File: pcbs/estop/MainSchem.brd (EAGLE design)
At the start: 94.9 x 61.8 mm, 41 parts, among them Q1 FDBL9401-F085, Q2 FDBL9401-F085, U1 FAN3100T, U2 FAN3100T

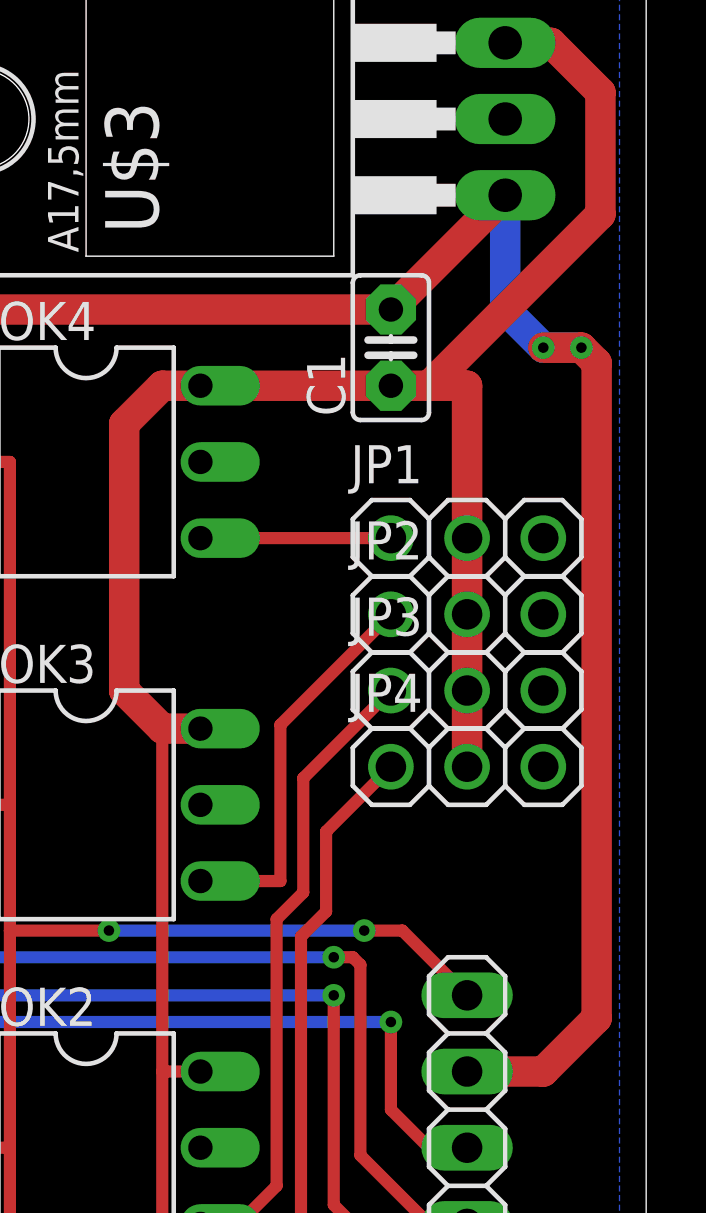
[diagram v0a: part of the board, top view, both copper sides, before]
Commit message: Fixed bugs in e-stop board for if I re-order them eventually.
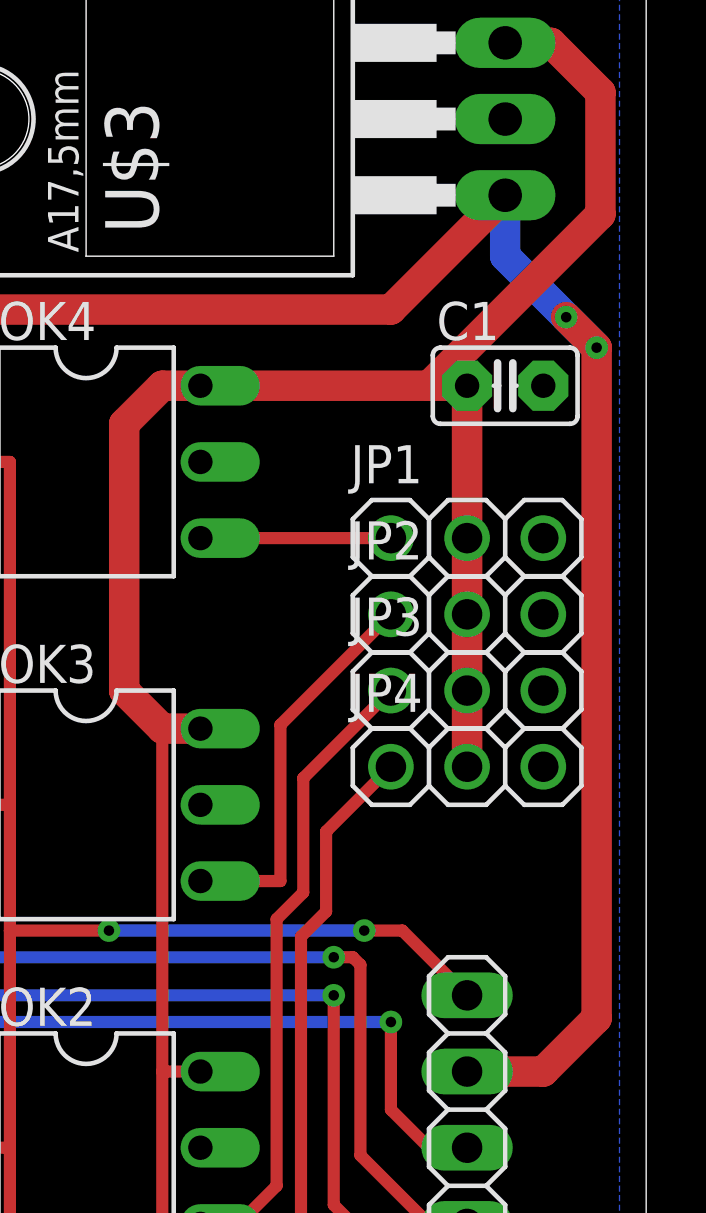
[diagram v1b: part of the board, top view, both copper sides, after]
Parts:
- moved C1 4.02 mm to (90.2, 47.0), turned to 0 degrees
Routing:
- net V+: track 146.0 -> 145.5 mm
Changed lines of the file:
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@@
 <layer number="25" name="tNames" color="7" fill="1" visible="yes" active="yes"/>
 <layer number="26" name="bNames" color="7" fill="1" visible="yes" active="yes"/>
-<layer number="27" name="tValues" color="7" fill="1" visible="yes" active="yes"/>
-<layer number="28" name="bValues" color="7" fill="1" visible="yes" active="yes"/>
-<layer number="29" name="tStop" color="7" fill="3" visible="yes" active="yes"/>
-<layer number="30" name="bStop" color="7" fill="6" visible="yes" active="yes"/>
+<layer number="27" name="tValues" color="7" fill="1" visible="no" active="yes"/>
+<layer number="28" name="bValues" color="7" fill="1" visible="no" active="yes"/>
+<layer number="29" name="tStop" color="7" fill="3" visible="no" active="yes"/>
+<layer number="30" name="bStop" color="7" fill="6" visible="no" active="yes"/>
 <layer number="31" name="tCream" color="7" fill="4" visible="no" active="yes"/>
 <layer number="32" name="bCream" color="7" fill="5" visible="no" active="yes"/>
@@
 <layer number="41" name="tRestrict" color="4" fill="10" visible="yes" active="yes"/>
 <layer number="42" name="bRestrict" color="1" fill="10" visible="yes" active="yes"/>
-<layer number="43" name="vRestrict" color="2" fill="10" visible="yes" active="yes"/>
+<layer number="43" name="vRestrict" color="2" fill="10" visible="no" active="yes"/>
 <layer number="44" name="Drills" color="7" fill="1" visible="no" active="yes"/>
 <layer number="45" name="Holes" color="7" fill="1" visible="no" active="yes"/>
 <layer number="46" name="Milling" color="3" fill="1" visible="no" active="yes"/>
 <layer number="47" name="Measures" color="7" fill="1" visible="no" active="yes"/>
-<layer number="48" name="Document" color="7" fill="1" visible="yes" active="yes"/>
-<layer number="49" name="Reference" color="7" fill="1" visible="yes" active="yes"/>
+<layer number="48" name="Document" color="7" fill="1" visible="no" active="yes"/>
+<layer number="49" name="Reference" color="7" fill="1" visible="no" active="yes"/>
 <layer number="50" name="dxf" color="7" fill="1" visible="no" active="no"/>
 <layer number="51" name="tDocu" color="7" fill="1" visible="yes" active="yes"/>
@@
 <layer number="127" name="_tValues" color="7" fill="1" visible="no" active="yes"/>
 <layer number="128" name="_bValues" color="7" fill="1" visible="no" active="yes"/>
-<layer number="129" name="Mask" color="7" fill="1" visible="yes" active="yes"/>
+<layer number="129" name="Mask" color="7" fill="1" visible="no" active="yes"/>
 <layer number="131" name="tAdjust" color="7" fill="1" visible="no" active="yes"/>
 <layer number="132" name="bAdjust" color="7" fill="1" visible="no" active="yes"/>
 <layer number="144" name="Drill_legend" color="7" fill="1" visible="no" active="yes"/>
-<layer number="150" name="Notes" color="7" fill="1" visible="yes" active="yes"/>
+<layer number="150" name="Notes" color="7" fill="1" visible="no" active="yes"/>
 <layer number="151" name="HeatSink" color="7" fill="1" visible="no" active="yes"/>
 <layer number="152" name="_bDocu" color="7" fill="1" visible="no" active="yes"/>
@@
 <layer number="223" name="223bmp" color="24" fill="1" visible="no" active="no"/>
 <layer number="224" name="224bmp" color="25" fill="1" visible="no" active="no"/>
-<layer number="225" name="225bmp" color="7" fill="1" visible="yes" active="yes"/>
-<layer number="226" name="226bmp" color="7" fill="1" visible="yes" active="yes"/>
-<layer number="227" name="227bmp" color="7" fill="1" visible="yes" active="yes"/>
-<layer number="228" name="228bmp" color="7" fill="1" visible="yes" active="yes"/>
-<layer number="229" name="229bmp" color="7" fill="1" visible="yes" active="yes"/>
-<layer number="230" name="230bmp" color="7" fill="1" visible="yes" active="yes"/>
+<layer number="225" name="225bmp" color="7" fill="1" visible="no" active="yes"/>
+<layer number="226" name="226bmp" color="7" fill="1" visible="no" active="yes"/>
+<layer number="227" name="227bmp" color="7" fill="1" visible="no" active="yes"/>
+<layer number="228" name="228bmp" color="7" fill="1" visible="no" active="yes"/>
+<layer number="229" name="229bmp" color="7" fill="1" visible="no" active="yes"/>
+<layer number="230" name="230bmp" color="7" fill="1" visible="no" active="yes"/>
 <layer number="231" name="Eagle3D_PG1" color="7" fill="1" visible="no" active="no"/>
 <layer number="232" name="Eagle3D_PG2" color="7" fill="1" visible="no" active="no"/>
@@
 <layer number="251" name="SMDround" color="7" fill="1" visible="no" active="no"/>
 <layer number="254" name="cooling" color="7" fill="1" visible="no" active="yes"/>
-<layer number="255" name="routoute" color="7" fill="1" visible="yes" active="yes"/>
+<layer number="255" name="routoute" color="7" fill="1" visible="no" active="yes"/>
 </layers>
 <board>
@@
 <vertex x="2.54" y="21.59"/>
 <vertex x="3.81" y="20.32"/>
-<vertex x="8.89" y="20.32"/>
-<vertex x="10.16" y="21.59"/>
-<vertex x="12.7" y="21.59"/>
 <vertex x="13.97" y="20.32"/>
 <vertex x="13.97" y="17.78"/>
@@
 <polygon width="0.0254" layer="30">
 <vertex x="13.97" y="22.86"/>
-<vertex x="12.7" y="21.59"/>
-<vertex x="12.7" y="20.32"/>
-<vertex x="10.16" y="20.32"/>
-<vertex x="10.16" y="21.59"/>
-<vertex x="8.89" y="22.86"/>
 <vertex x="1.27" y="22.86"/>
 <vertex x="1.27" y="35.56"/>
@@
 <vertex x="37.338" y="17.018"/>
 <vertex x="37.338" y="19.812"/>
+</polygon>
+<polygon width="0.0254" layer="30">
+<vertex x="3.556" y="23.114"/>
+<vertex x="5.08" y="21.59"/>
+<vertex x="3.556" y="20.066"/>
+<vertex x="9.144" y="20.066"/>
+<vertex x="7.62" y="21.59"/>
+<vertex x="9.144" y="23.114"/>
+<vertex x="13.716" y="23.114"/>
+<vertex x="15.24" y="21.59"/>
+<vertex x="13.716" y="20.066"/>
+<vertex x="13.716" y="17.78"/>
+<vertex x="15.494" y="16.002"/>
+<vertex x="19.558" y="20.066"/>
+<vertex x="19.558" y="24.638"/>
+<vertex x="13.97" y="30.226"/>
+<vertex x="3.302" y="30.226"/>
+<vertex x="3.556" y="29.972"/>
 </polygon>
 </plain>
@@
 </autorouter>
 <elements>
-<element name="C1" library="adafruit" library_urn="urn:adsk.eagle:library:420" package="C025-025X050" package3d_urn="urn:adsk.eagle:package:6240323/1" value="" x="86.36" y="48.26" smashed="yes" rot="R90">
-<attribute name="NAME" x="84.836" y="45.974" size="1.27" layer="25" ratio="10" rot="R90"/>
-<attribute name="VALUE" x="89.154" y="45.974" size="1.27" layer="27" ratio="10" rot="R90"/>
+<element name="C1" library="adafruit" library_urn="urn:adsk.eagle:library:420" package="C025-025X050" package3d_urn="urn:adsk.eagle:package:6240323/1" value="" x="90.17" y="46.99" smashed="yes">
+<attribute name="NAME" x="87.884" y="48.514" size="1.27" layer="25" ratio="10"/>
+<attribute name="VALUE" x="87.884" y="44.196" size="1.27" layer="27" ratio="10"/>
 </element>
 <element name="JP1" library="adafruit" library_urn="urn:adsk.eagle:library:420" package="1X03" package3d_urn="urn:adsk.eagle:package:6240710/1" value="" x="88.9" y="41.91" smashed="yes">
@@
 <contactref element="U$10" pad="P$6"/>
 <contactref element="U$10" pad="P$3"/>
-<wire x1="90.17" y1="53.34" x2="90.17" y2="49.53" width="1.016" layer="16"/>
-<wire x1="90.17" y1="49.53" x2="91.44" y2="48.26" width="1.016" layer="16"/>
-<via x="91.44" y="48.26" extent="1-16" drill="0.35"/>
+<wire x1="90.17" y1="53.34" x2="90.17" y2="51.308" width="1.016" layer="16"/>
+<wire x1="90.17" y1="51.308" x2="92.202" y2="49.276" width="1.016" layer="16"/>
+<via x="92.202" y="49.276" extent="1-16" drill="0.35"/>
 <wire x1="93.218" y1="25.908" x2="91.44" y2="24.13" width="1.016" layer="1"/>
 <wire x1="91.44" y1="24.13" x2="88.9" y2="24.13" width="1.016" layer="1"/>
-<wire x1="93.218" y1="47.752" x2="93.218" y2="25.908" width="1.016" layer="1"/>
-<wire x1="91.44" y1="48.26" x2="92.71" y2="48.26" width="1.016" layer="16"/>
-<via x="92.71" y="48.26" extent="1-16" drill="0.35"/>
-<wire x1="92.71" y1="48.26" x2="91.44" y2="48.26" width="1.016" layer="1"/>
-<wire x1="92.71" y1="48.26" x2="93.218" y2="47.752" width="1.016" layer="1"/>
+<wire x1="93.218" y1="48.26" x2="93.218" y2="25.908" width="1.016" layer="1"/>
+<wire x1="92.202" y1="49.276" x2="93.218" y2="48.26" width="1.016" layer="16"/>
+<via x="93.218" y="48.26" extent="1-16" drill="0.35"/>
+<wire x1="93.218" y1="48.26" x2="92.202" y2="49.276" width="1.016" layer="1"/>
 <wire x1="90.17" y1="53.34" x2="86.36" y2="49.53" width="1.016" layer="1"/>
 <contactref element="U$15" pad="P$7"/>
@@
 <wire x1="93.345" y1="52.705" x2="87.63" y2="46.99" width="1.016" layer="1"/>
 <wire x1="90.17" y1="58.42" x2="91.694" y2="58.42" width="1.016" layer="1"/>
-<wire x1="88.9" y1="41.91" x2="86.36" y2="46.99" width="0" layer="19" extent="1-1"/>
 </signal>
 </signals>

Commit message: Increased e-stop <-> interposer ribbon cable drill size to make soldering the ribbon cable easier in future versions.
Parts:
- JP7: device pinhead:1X08 -> HighCurrentTransistorAndDriver:1X08_RIBBONCABLE
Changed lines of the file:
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@@
 <attribute name="VALUE" x="48.26" y="16.51" size="1.27" layer="27"/>
 </element>
-<element name="JP7" library="pinhead" library_urn="urn:adsk.eagle:library:325" package="1X08" package3d_urn="urn:adsk.eagle:package:22409/2" value="" x="88.9" y="17.78" smashed="yes" rot="R90">
+<element name="JP7" library="HighCurrentTransistorAndDriver" package="1X08_RIBBONCABLE" package3d_urn="urn:adsk.eagle:package:22409/2" value="" x="88.9" y="17.78" smashed="yes" rot="R90">
 <attribute name="NAME" x="87.0712" y="6.2738" size="1.27" layer="25" ratio="10" rot="R90"/>
 <attribute name="POPULARITY" value="67" x="88.9" y="17.78" size="1.778" layer="27" rot="R90" display="off"/>
